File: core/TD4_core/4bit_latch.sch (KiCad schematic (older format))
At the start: 4 parts

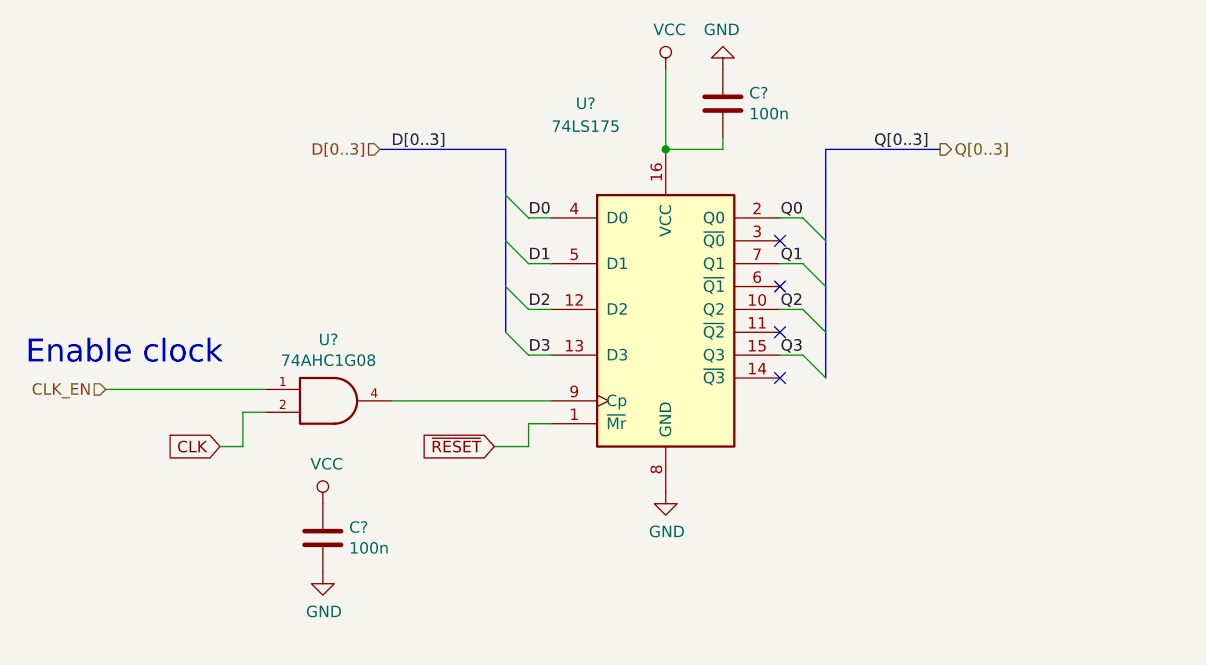
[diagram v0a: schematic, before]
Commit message: Core assembled; decoder left
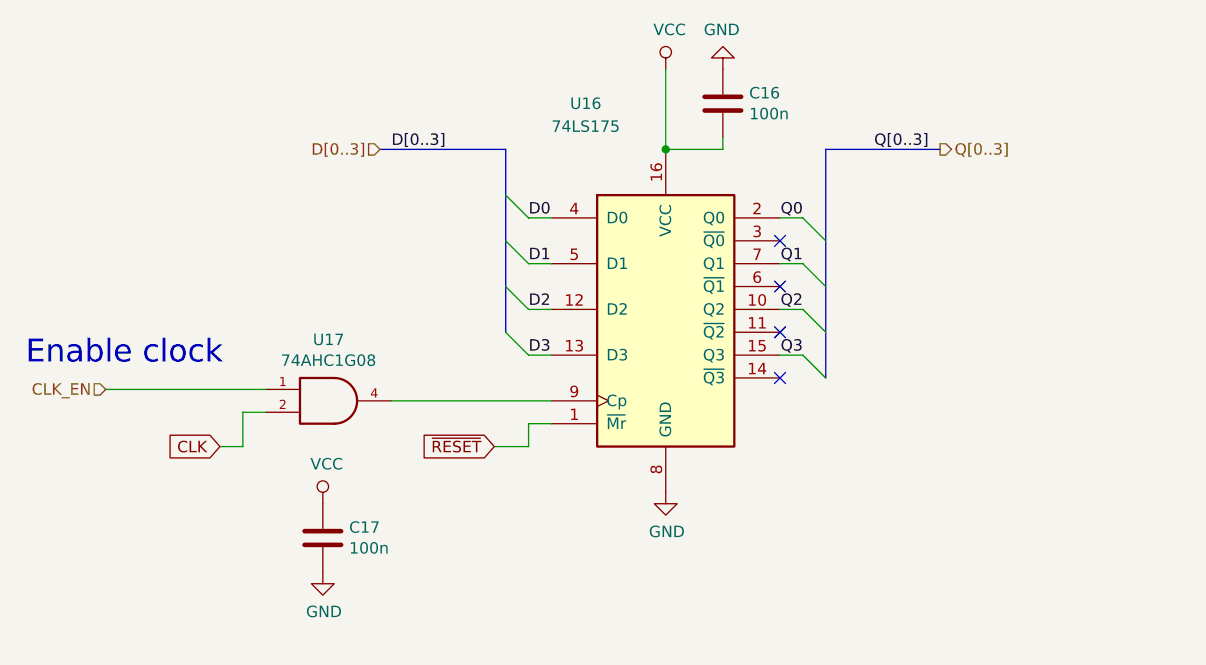
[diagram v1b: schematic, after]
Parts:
- gave numbers to parts that had none: 4
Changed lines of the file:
@@
 $EndDescr
 $Comp
-L 74xx:74LS175 U?
+L 74xx:74LS175 U13
 U 1 1 5C63082C
 P 5850 3650
-AR Path="/5C63072E/5C63082C" Ref="U?"  Part="1"
+AR Path="/5C63072E/5C63082C" Ref="U13"  Part="1"
 AR Path="/5C63A7FA/5C63082C" Ref="U?"  Part="1"
-AR Path="/5C685283/5C63082C" Ref="U?"  Part="1"
-F 0 "U?" H 5500 4550 50  0000 C CNN
+AR Path="/5C685283/5C63082C" Ref="U16"  Part="1"
+F 0 "U16" H 5500 4550 50  0000 C CNN
 F 1 "74LS175" H 5500 4450 50  0000 C CNN
 F 2 "" H 5850 3650 50  0001 C CNN
@@
 $EndComp
 $Comp
-L Device:C C?
+L Device:C C13
 U 1 1 5C6310BA
 P 6100 2750
-AR Path="/5C63072E/5C6310BA" Ref="C?"  Part="1"
+AR Path="/5C63072E/5C6310BA" Ref="C13"  Part="1"
 AR Path="/5C63A7FA/5C6310BA" Ref="C?"  Part="1"
-AR Path="/5C685283/5C6310BA" Ref="C?"  Part="1"
-F 0 "C?" H 6215 2796 50  0000 L CNN
+AR Path="/5C685283/5C6310BA" Ref="C16"  Part="1"
+F 0 "C16" H 6215 2796 50  0000 L CNN
 F 1 "100n" H 6215 2705 50  0000 L CNN
 F 2 "" H 6138 2600 50  0001 C CNN
@@
 $EndComp
 $Comp
-L power:GND #PWR?
+L power:GND #PWR0127
 U 1 1 5C631117
 P 6100 2600
-AR Path="/5C63072E/5C631117" Ref="#PWR?"  Part="1"
+AR Path="/5C63072E/5C631117" Ref="#PWR0127"  Part="1"
 AR Path="/5C63A7FA/5C631117" Ref="#PWR?"  Part="1"
-AR Path="/5C685283/5C631117" Ref="#PWR?"  Part="1"
-F 0 "#PWR?" H 6100 2350 50  0001 C CNN
+AR Path="/5C685283/5C631117" Ref="#PWR0134"  Part="1"
+F 0 "#PWR0134" H 6100 2350 50  0001 C CNN
 F 1 "GND" H 6105 2427 50  0000 C CNN
 F 2 "" H 6100 2600 50  0001 C CNN
@@
 $EndComp
 $Comp
-L power:VCC #PWR?
+L power:VCC #PWR0128
 U 1 1 5C631158
 P 5850 2600
-AR Path="/5C63072E/5C631158" Ref="#PWR?"  Part="1"
+AR Path="/5C63072E/5C631158" Ref="#PWR0128"  Part="1"
 AR Path="/5C63A7FA/5C631158" Ref="#PWR?"  Part="1"
-AR Path="/5C685283/5C631158" Ref="#PWR?"  Part="1"
-F 0 "#PWR?" H 5850 2450 50  0001 C CNN
+AR Path="/5C685283/5C631158" Ref="#PWR0135"  Part="1"
+F 0 "#PWR0135" H 5850 2450 50  0001 C CNN
 F 1 "VCC" H 5867 2773 50  0000 C CNN
 F 2 "" H 5850 2600 50  0001 C CNN
@@
 Connection ~ 5850 2950
 $Comp
-L power:GND #PWR?
+L power:GND #PWR0129
 U 1 1 5C6319CE
 P 5850 4450
-AR Path="/5C63072E/5C6319CE" Ref="#PWR?"  Part="1"
+AR Path="/5C63072E/5C6319CE" Ref="#PWR0129"  Part="1"
 AR Path="/5C63A7FA/5C6319CE" Ref="#PWR?"  Part="1"
-AR Path="/5C685283/5C6319CE" Ref="#PWR?"  Part="1"
-F 0 "#PWR?" H 5850 4200 50  0001 C CNN
+AR Path="/5C685283/5C6319CE" Ref="#PWR0136"  Part="1"
+F 0 "#PWR0136" H 5850 4200 50  0001 C CNN
 F 1 "GND" H 5855 4277 50  0000 C CNN
 F 2 "" H 5850 4450 50  0001 C CNN
@@
 	5250 4150 5350 4150
 $Comp
-L 74xGxx:74AHC1G08 U?
+L 74xGxx:74AHC1G08 U14
 U 1 1 5C6359C2
 P 4400 4050
-AR Path="/5C63072E/5C6359C2" Ref="U?"  Part="1"
+AR Path="/5C63072E/5C6359C2" Ref="U14"  Part="1"
 AR Path="/5C63A7FA/5C6359C2" Ref="U?"  Part="1"
-AR Path="/5C685283/5C6359C2" Ref="U?"  Part="1"
-F 0 "U?" H 4375 4317 50  0000 C CNN
+AR Path="/5C685283/5C6359C2" Ref="U17"  Part="1"
+F 0 "U17" H 4375 4317 50  0000 C CNN
 F 1 "74AHC1G08" H 4375 4226 50  0000 C CNN
 F 2 "" H 4400 4050 50  0001 C CNN
@@
 P 4350 4650
 AR Path="/5C63A7FA/5C6615CC" Ref="C?"  Part="1"
-AR Path="/5C63072E/5C6615CC" Ref="C?"  Part="1"
-AR Path="/5C685283/5C6615CC" Ref="C?"  Part="1"
-F 0 "C?" H 4465 4696 50  0000 L CNN
+AR Path="/5C63072E/5C6615CC" Ref="C14"  Part="1"
+AR Path="/5C685283/5C6615CC" Ref="C17"  Part="1"
+F 0 "C17" H 4465 4696 50  0000 L CNN
 F 1 "100n" H 4465 4605 50  0000 L CNN
 F 2 "" H 4388 4500 50  0001 C CNN
@@
 P 4350 4800
 AR Path="/5C63A7FA/5C66162D" Ref="#PWR?"  Part="1"
-AR Path="/5C63072E/5C66162D" Ref="#PWR?"  Part="1"
-AR Path="/5C685283/5C66162D" Ref="#PWR?"  Part="1"
-F 0 "#PWR?" H 4350 4550 50  0001 C CNN
+AR Path="/5C63072E/5C66162D" Ref="#PWR0130"  Part="1"
+AR Path="/5C685283/5C66162D" Ref="#PWR0137"  Part="1"
+F 0 "#PWR0137" H 4350 4550 50  0001 C CNN
 F 1 "GND" H 4355 4627 50  0000 C CNN
 F 2 "" H 4350 4800 50  0001 C CNN
@@
 P 4350 4500
 AR Path="/5C63A7FA/5C661670" Ref="#PWR?"  Part="1"
-AR Path="/5C63072E/5C661670" Ref="#PWR?"  Part="1"
-AR Path="/5C685283/5C661670" Ref="#PWR?"  Part="1"
-F 0 "#PWR?" H 4350 4350 50  0001 C CNN
+AR Path="/5C63072E/5C661670" Ref="#PWR0131"  Part="1"
+AR Path="/5C685283/5C661670" Ref="#PWR0138"  Part="1"
+F 0 "#PWR0138" H 4350 4350 50  0001 C CNN
 F 1 "VCC" H 4367 4673 50  0000 C CNN
 F 2 "" H 4350 4500 50  0001 C CNN

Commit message: Decoder done (finally!)
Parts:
- U32: renamed from U13; value 74LS175 -> 74HC175
- renumbered C13 to C32, C14 to C33, U14 to U33
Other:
- moved on the sheet: C36
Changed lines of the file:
@@
 $Descr A4 11693 8268
 encoding utf-8
-Sheet 8 9
+Sheet 22 23
 Title ""
 Date ""
@@
 $EndDescr
 $Comp
-L 74xx:74LS175 U13
+L 74xx:74LS175 U32
 U 1 1 5C63082C
 P 5850 3650
-AR Path="/5C63072E/5C63082C" Ref="U13"  Part="1"
+AR Path="/5C63072E/5C63082C" Ref="U32"  Part="1"
 AR Path="/5C63A7FA/5C63082C" Ref="U?"  Part="1"
-AR Path="/5C685283/5C63082C" Ref="U16"  Part="1"
-F 0 "U16" H 5500 4550 50  0000 C CNN
-F 1 "74LS175" H 5500 4450 50  0000 C CNN
+AR Path="/5C685283/5C63082C" Ref="U35"  Part="1"
+F 0 "U35" H 5500 4550 50  0000 C CNN
+F 1 "74HC175" H 5500 4450 50  0000 C CNN
 F 2 "" H 5850 3650 50  0001 C CNN
 F 3 "http://www.ti.com/lit/gpn/sn74LS175" H 5850 3650 50  0001 C CNN
@@
 $EndComp
 $Comp
-L Device:C C13
+L Device:C C32
 U 1 1 5C6310BA
 P 6100 2750
-AR Path="/5C63072E/5C6310BA" Ref="C13"  Part="1"
+AR Path="/5C63072E/5C6310BA" Ref="C32"  Part="1"
 AR Path="/5C63A7FA/5C6310BA" Ref="C?"  Part="1"
-AR Path="/5C685283/5C6310BA" Ref="C16"  Part="1"
-F 0 "C16" H 6215 2796 50  0000 L CNN
+AR Path="/5C685283/5C6310BA" Ref="C35"  Part="1"
+F 0 "C35" H 6215 2796 50  0000 L CNN
 F 1 "100n" H 6215 2705 50  0000 L CNN
 F 2 "" H 6138 2600 50  0001 C CNN
@@
 $EndComp
 $Comp
-L power:GND #PWR0127
+L power:GND #PWR0107
 U 1 1 5C631117
 P 6100 2600
-AR Path="/5C63072E/5C631117" Ref="#PWR0127"  Part="1"
+AR Path="/5C63072E/5C631117" Ref="#PWR0107"  Part="1"
 AR Path="/5C63A7FA/5C631117" Ref="#PWR?"  Part="1"
-AR Path="/5C685283/5C631117" Ref="#PWR0134"  Part="1"
-F 0 "#PWR0134" H 6100 2350 50  0001 C CNN
+AR Path="/5C685283/5C631117" Ref="#PWR0116"  Part="1"
+F 0 "#PWR0116" H 6100 2350 50  0001 C CNN
 F 1 "GND" H 6105 2427 50  0000 C CNN
 F 2 "" H 6100 2600 50  0001 C CNN
@@
 $EndComp
 $Comp
-L power:VCC #PWR0128
+L power:VCC #PWR0106
 U 1 1 5C631158
 P 5850 2600
-AR Path="/5C63072E/5C631158" Ref="#PWR0128"  Part="1"
+AR Path="/5C63072E/5C631158" Ref="#PWR0106"  Part="1"
 AR Path="/5C63A7FA/5C631158" Ref="#PWR?"  Part="1"
-AR Path="/5C685283/5C631158" Ref="#PWR0135"  Part="1"
-F 0 "#PWR0135" H 5850 2450 50  0001 C CNN
+AR Path="/5C685283/5C631158" Ref="#PWR0115"  Part="1"
+F 0 "#PWR0115" H 5850 2450 50  0001 C CNN
 F 1 "VCC" H 5867 2773 50  0000 C CNN
 F 2 "" H 5850 2600 50  0001 C CNN
@@
 Connection ~ 5850 2950
 $Comp
-L power:GND #PWR0129
+L power:GND #PWR0110
 U 1 1 5C6319CE
 P 5850 4450
-AR Path="/5C63072E/5C6319CE" Ref="#PWR0129"  Part="1"
+AR Path="/5C63072E/5C6319CE" Ref="#PWR0110"  Part="1"
 AR Path="/5C63A7FA/5C6319CE" Ref="#PWR?"  Part="1"
-AR Path="/5C685283/5C6319CE" Ref="#PWR0136"  Part="1"
-F 0 "#PWR0136" H 5850 4200 50  0001 C CNN
+AR Path="/5C685283/5C6319CE" Ref="#PWR0119"  Part="1"
+F 0 "#PWR0119" H 5850 4200 50  0001 C CNN
 F 1 "GND" H 5855 4277 50  0000 C CNN
 F 2 "" H 5850 4450 50  0001 C CNN
@@
 	5250 4150 5350 4150
 $Comp
-L 74xGxx:74AHC1G08 U14
+L 74xGxx:74AHC1G08 U33
 U 1 1 5C6359C2
 P 4400 4050
-AR Path="/5C63072E/5C6359C2" Ref="U14"  Part="1"
+AR Path="/5C63072E/5C6359C2" Ref="U33"  Part="1"
 AR Path="/5C63A7FA/5C6359C2" Ref="U?"  Part="1"
-AR Path="/5C685283/5C6359C2" Ref="U17"  Part="1"
-F 0 "U17" H 4375 4317 50  0000 C CNN
-F 1 "74AHC1G08" H 4375 4226 50  0000 C CNN
+AR Path="/5C685283/5C6359C2" Ref="U36"  Part="1"
+F 0 "U36" H 4400 4400 50  0000 C CNN
+F 1 "74AHC1G08" H 4400 4300 50  0000 C CNN
 F 2 "" H 4400 4050 50  0001 C CNN
 F 3 "http://www.ti.com/lit/sg/scyt129e/scyt129e.pdf" H 4400 4050 50  0001 C CNN
@@
 Wire Bus Line
 	6550 2950 7050 2950
-Wire Bus Line
-	5150 2950 5150 3750
-Wire Bus Line
-	6550 2950 6550 3950
 Text HLabel 4600 2950 0    50   Input ~ 0
 D[0..3]
@@
 L Device:C C?
 U 1 1 5C6615CC
-P 4350 4650
+P 7800 4750
 AR Path="/5C63A7FA/5C6615CC" Ref="C?"  Part="1"
-AR Path="/5C63072E/5C6615CC" Ref="C14"  Part="1"
-AR Path="/5C685283/5C6615CC" Ref="C17"  Part="1"
-F 0 "C17" H 4465 4696 50  0000 L CNN
-F 1 "100n" H 4465 4605 50  0000 L CNN
-F 2 "" H 4388 4500 50  0001 C CNN
-F 3 "~" H 4350 4650 50  0001 C CNN
-	1    4350 4650
+AR Path="/5C63072E/5C6615CC" Ref="C33"  Part="1"
+AR Path="/5C685283/5C6615CC" Ref="C36"  Part="1"
+F 0 "C36" H 7915 4796 50  0000 L CNN
+F 1 "100n" H 7915 4705 50  0000 L CNN
+F 2 "" H 7838 4600 50  0001 C CNN
+F 3 "~" H 7800 4750 50  0001 C CNN
+	1    7800 4750
 	1    0    0    -1
 $EndComp
@@
 L power:GND #PWR?
 U 1 1 5C66162D
-P 4350 4800
+P 7800 4900
 AR Path="/5C63A7FA/5C66162D" Ref="#PWR?"  Part="1"
-AR Path="/5C63072E/5C66162D" Ref="#PWR0130"  Part="1"
-AR Path="/5C685283/5C66162D" Ref="#PWR0137"  Part="1"
-F 0 "#PWR0137" H 4350 4550 50  0001 C CNN
-F 1 "GND" H 4355 4627 50  0000 C CNN
-F 2 "" H 4350 4800 50  0001 C CNN
-F 3 "" H 4350 4800 50  0001 C CNN
-	1    4350 4800
+AR Path="/5C63072E/5C66162D" Ref="#PWR0112"  Part="1"
+AR Path="/5C685283/5C66162D" Ref="#PWR0121"  Part="1"
+F 0 "#PWR0121" H 7800 4650 50  0001 C CNN
+F 1 "GND" H 7805 4727 50  0000 C CNN
+F 2 "" H 7800 4900 50  0001 C CNN
+F 3 "" H 7800 4900 50  0001 C CNN
+	1    7800 4900
 	1    0    0    -1
 $EndComp
@@
 L power:VCC #PWR?
 U 1 1 5C661670
-P 4350 4500
+P 7800 4600
 AR Path="/5C63A7FA/5C661670" Ref="#PWR?"  Part="1"
-AR Path="/5C63072E/5C661670" Ref="#PWR0131"  Part="1"
-AR Path="/5C685283/5C661670" Ref="#PWR0138"  Part="1"
-F 0 "#PWR0138" H 4350 4350 50  0001 C CNN
-F 1 "VCC" H 4367 4673 50  0000 C CNN
-F 2 "" H 4350 4500 50  0001 C CNN
-F 3 "" H 4350 4500 50  0001 C CNN
-	1    4350 4500
-	1    0    0    -1
-$EndComp
+AR Path="/5C63072E/5C661670" Ref="#PWR0111"  Part="1"
+AR Path="/5C685283/5C661670" Ref="#PWR0120"  Part="1"
+F 0 "#PWR0120" H 7800 4450 50  0001 C CNN
+F 1 "VCC" H 7817 4773 50  0000 C CNN
+F 2 "" H 7800 4600 50  0001 C CNN
+F 3 "" H 7800 4600 50  0001 C CNN
+	1    7800 4600
+	1    0    0    -1
+$EndComp
+Wire Bus Line
+	5150 2950 5150 3750
+Wire Bus Line
+	6550 2950 6550 3950
+$Comp
+L power:GND #PWR0118
+U 1 1 5C75DE80
+P 4400 4150
+AR Path="/5C685283/5C75DE80" Ref="#PWR0118"  Part="1"
+AR Path="/5C63072E/5C75DE80" Ref="#PWR0109"  Part="1"
+F 0 "#PWR0118" H 4400 3900 50  0001 C CNN
+F 1 "GND" H 4405 3977 50  0001 C CNN
+F 2 "" H 4400 4150 50  0001 C CNN
+F 3 "" H 4400 4150 50  0001 C CNN
+	1    4400 4150
+	1    0    0    -1
+$EndComp
+$Comp
+L power:VCC #PWR0117
+U 1 1 5C75DEC3
+P 4400 3950
+AR Path="/5C685283/5C75DEC3" Ref="#PWR0117"  Part="1"
+AR Path="/5C63072E/5C75DEC3" Ref="#PWR0108"  Part="1"
+F 0 "#PWR0117" H 4400 3800 50  0001 C CNN
+F 1 "VCC" H 4417 4123 50  0001 C CNN
+F 2 "" H 4400 3950 50  0001 C CNN
+F 3 "" H 4400 3950 50  0001 C CNN
+	1    4400 3950
+	1    0    0    -1
+$EndComp
